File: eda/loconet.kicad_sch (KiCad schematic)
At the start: 68 parts, among them J1 RJ12, J10 FROG4, J11 LN Debug, J12 LN Raw, J13 12V IN, J2 DCC IN, J3 FROG1, J4 DCC1, J5 FROG2, J6 DCC2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

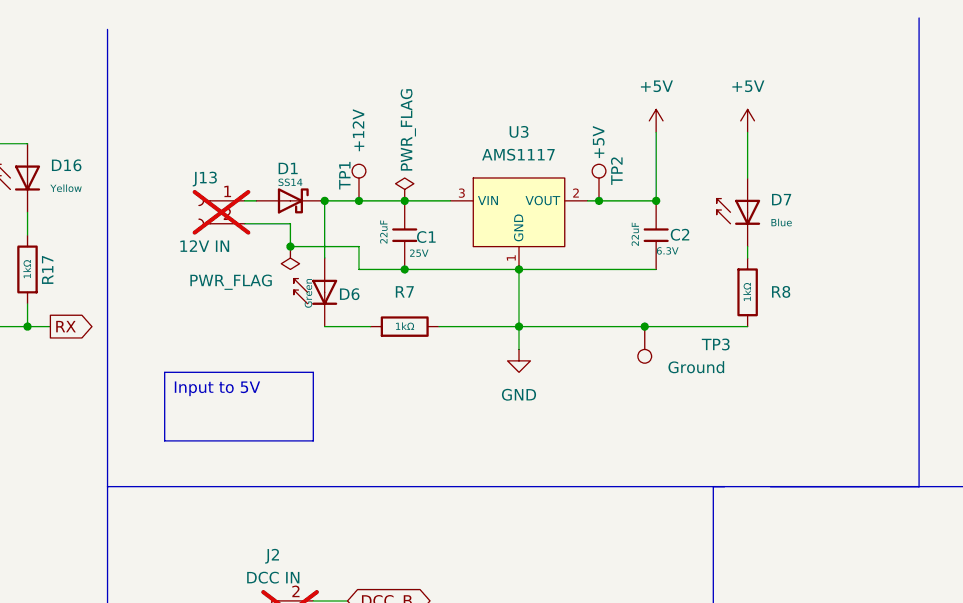
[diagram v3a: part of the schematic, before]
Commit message: Design fixups
* LDO was too limited in input voltage, switch to a part with a bigger input voltage
* Update README
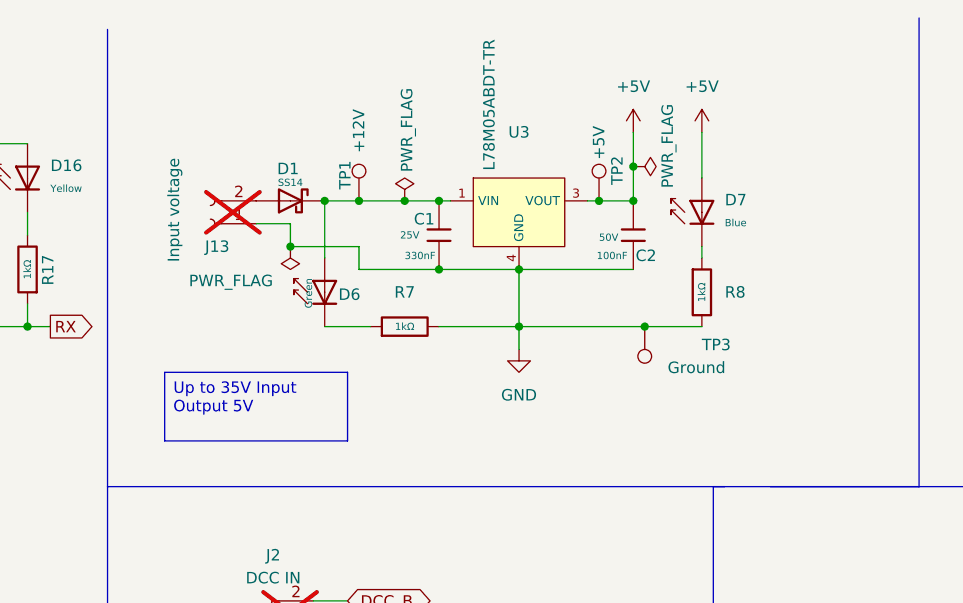
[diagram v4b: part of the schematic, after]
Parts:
- removed C1: 22uF, PCM_JLCPCB:C_0805, symbol PCM_JLCPCB-Capacitors:0805,22uF
- removed C2: 22uF, PCM_JLCPCB:C_0603, symbol PCM_JLCPCB-Capacitors:0603,22uF
- removed U3: AMS1117, PCM_JLCPCB:SOT-223_L6.5-W3.5-P2.30-LS7.0-BR, symbol PCM_JLCPCB-Power:LDO, 5V, 1A
- added C1: 330nF, PCM_JLCPCB:C_0603, symbol PCM_JLCPCB-Capacitors:0603,330nF
- added C2: 100nF, PCM_JLCPCB:C_0603, symbol PCM_JLCPCB-Capacitors:0603,100nF
- added U3: L78M05ABDT-TR, PCM_JLCPCB:TO-252-2_L6.5-W6.1-P4.58-LS10.0-TL, symbol PCM_JLCPCB-Power:LDO, 5V, 0.5A
- J13: value 12V IN -> Input voltage
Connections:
- net +5V: now also C2.1, U3.3 (VOUT)
- net GND: now also J13.1 (Pin_1), C1.2, C2.2, U3.4 (GND); no longer J13.2 (Pin_2)
- net at D1.2: now also J13.2 (Pin_2); no longer J13.1 (Pin_1)
- net at D1.1, D6.2, TP1.1: now also C1.1, U3.1 (VIN)
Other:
- moved on the sheet: D7, J13, R8

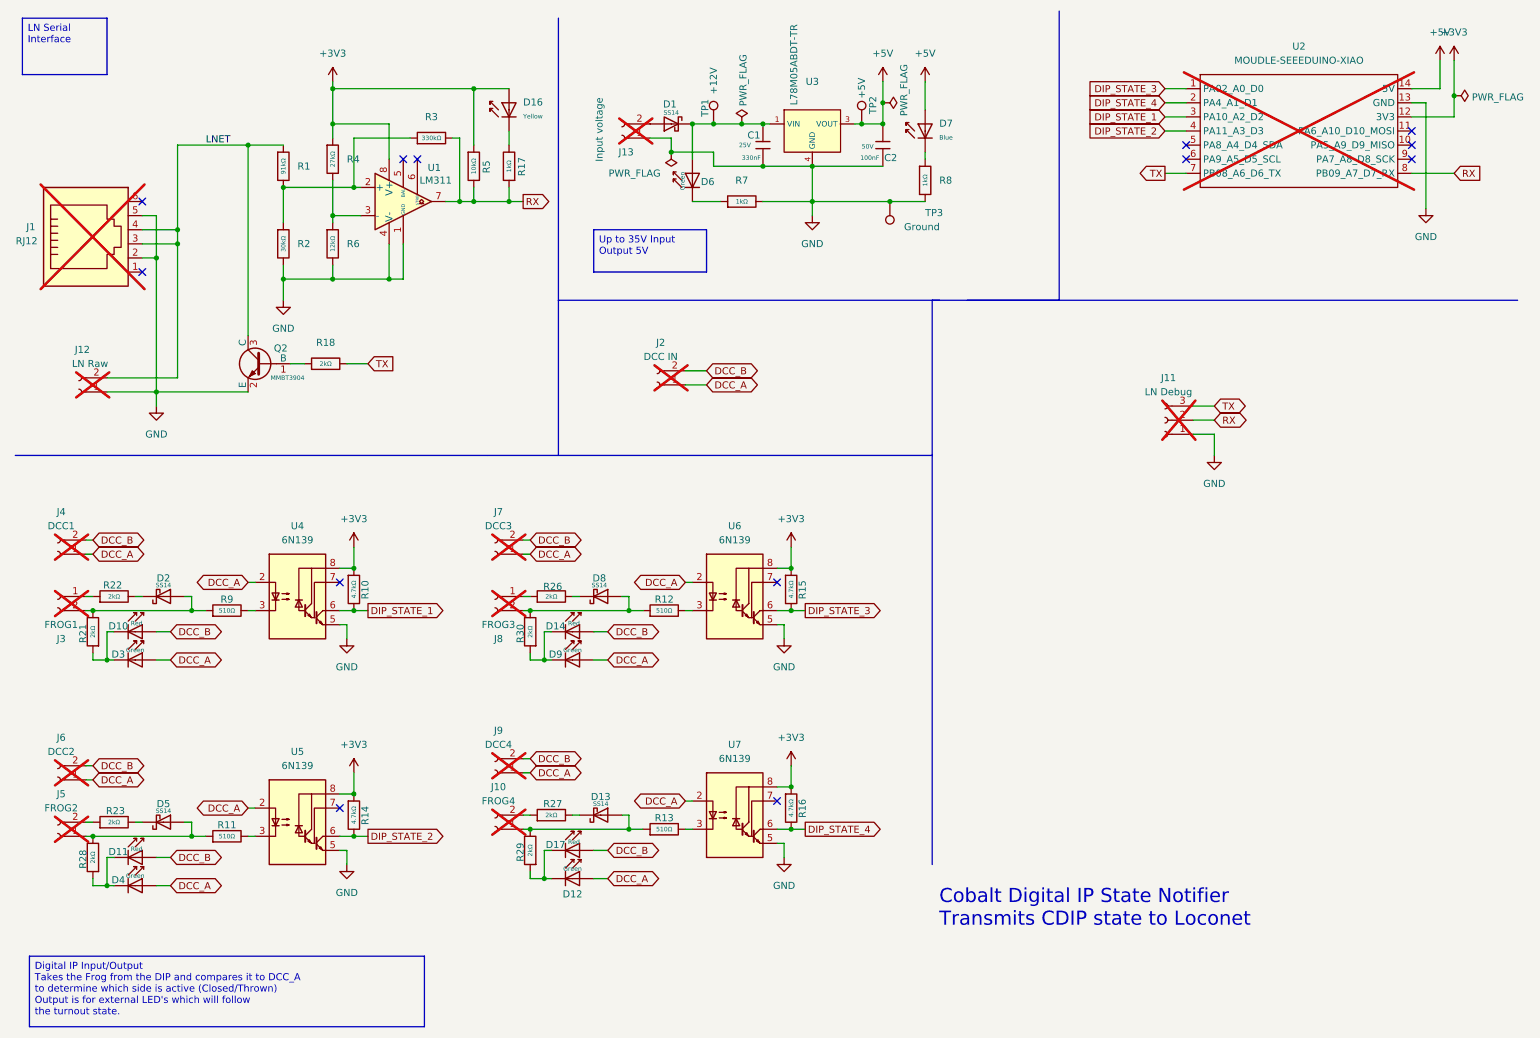
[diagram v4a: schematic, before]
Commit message: Updates
* Made it possible to power with DCC. You still need a DCC input for the IO, but you can also drive this with DCC.
* Added some screen printing for help
* Added 3 GPIO headers. You can connect them how you want, but they aren't protected, so don't do anything dumb.
* updated readme
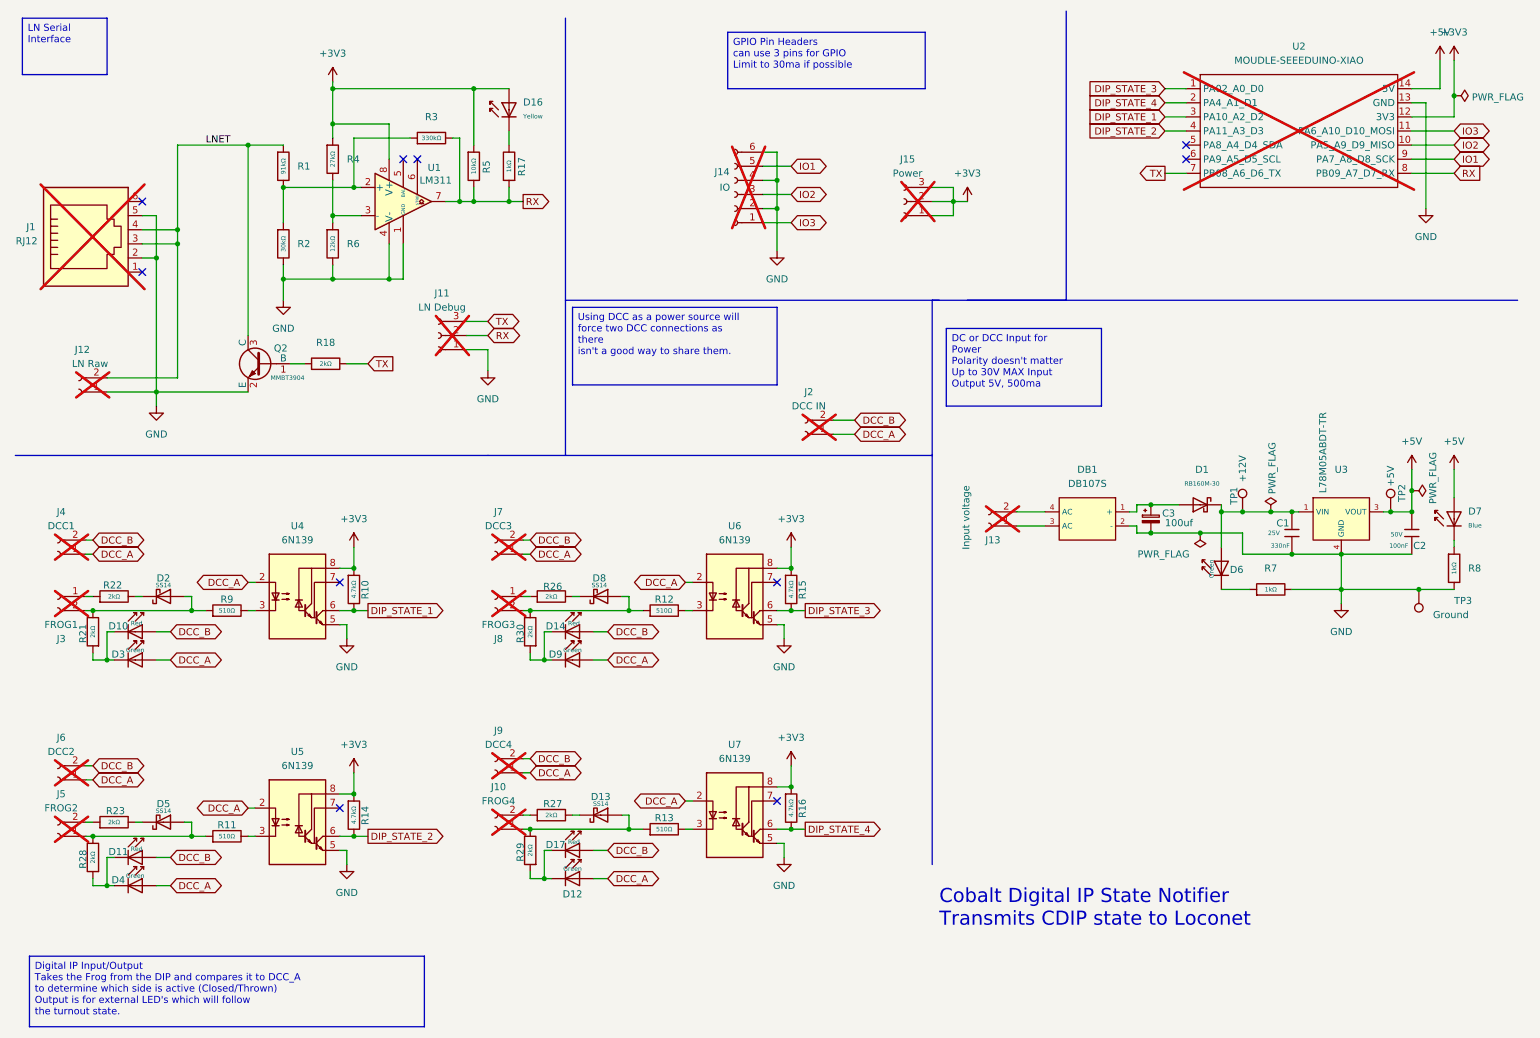
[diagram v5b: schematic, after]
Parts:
- removed D1: SS14, PCM_JLCPCB:D_SMA, symbol PCM_JLCPCB-Diodes:Schottky,SS14
- added C3: 100uf, Capacitor_THT:CP_Radial_D5.0mm_P2.50mm, symbol Device:C_Polarized_Small
- added D1: RB160M-30, PCM_JLCPCB:D_SOD-123, symbol PCM_JLCPCB-Diodes:Schottky,RB160M-30
- added DB1: DB107S, PCM_JLCPCB:DBS_L8.2-W6.4-P5.10-LS10.0-BL, symbol PCM_JLCPCB-Diode-Packages:Bridge Rectifier, DB107S
- added J14: IO, Connector_PinHeader_2.54mm:PinHeader_2x03_P2.54mm_Vertical, symbol Connector:Conn_01x06_Socket
- added J15: Power, Connector_PinHeader_2.54mm:PinHeader_1x03_P2.54mm_Vertical, symbol Connector:Conn_01x03_Socket
- J1: footprint Connector_RJ:RJ12_Amphenol_54601-x06_Horizontal -> Connector_RJ:RJ25_Wayconn_MJEA-660X1_Horizontal
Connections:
- net +3V3: now also J15.1 (Pin_1), J15.2 (Pin_2), J15.3 (Pin_3)
- net GND: now also C3.2, DB1.2 (-), J14.2 (Pin_2), J14.4 (Pin_4), J14.6 (Pin_6); no longer J13.1 (Pin_1)
- net at J13.2 (Pin_2): now also DB1.4 (AC)
- net at C1.1, D6.2, TP1.1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: now also D1.1
- net IO2: now reaches U2.10 (PA5_A9_D9_MISO)
- net IO2: now also J14.3 (Pin_3)
- net IO3: now reaches U2.11 (PA6_A10_D10_MOSI)
- net IO3: now also J14.1 (Pin_1)
- net IO1: now reaches U2.9 (PA7_A8_D8_SCK)
- net IO1: now also J14.5 (Pin_5)
- new net: C3.1, D1.2, DB1.1 (+)
- new net: DB1.3 (AC), J13.1 (Pin_1)
- no-connect marks 13 -> 10
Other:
- moved on the sheet: C1, C2, D6, D7, J11, J13, J2, R7, R8, TP1, TP2, TP3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

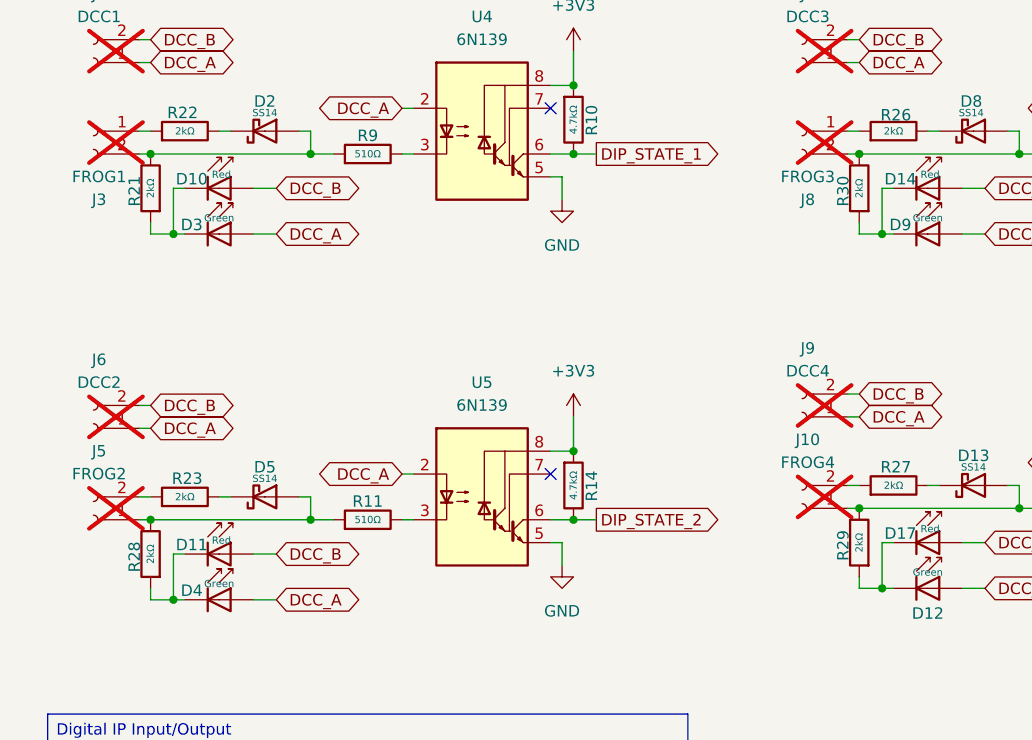
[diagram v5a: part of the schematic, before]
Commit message: Fixes
* Bumped the turnout indicator LED resistor to a 125mw 0805 as the 62.5mw was likely going to be too small. This allows some headroom.
* Updated README.
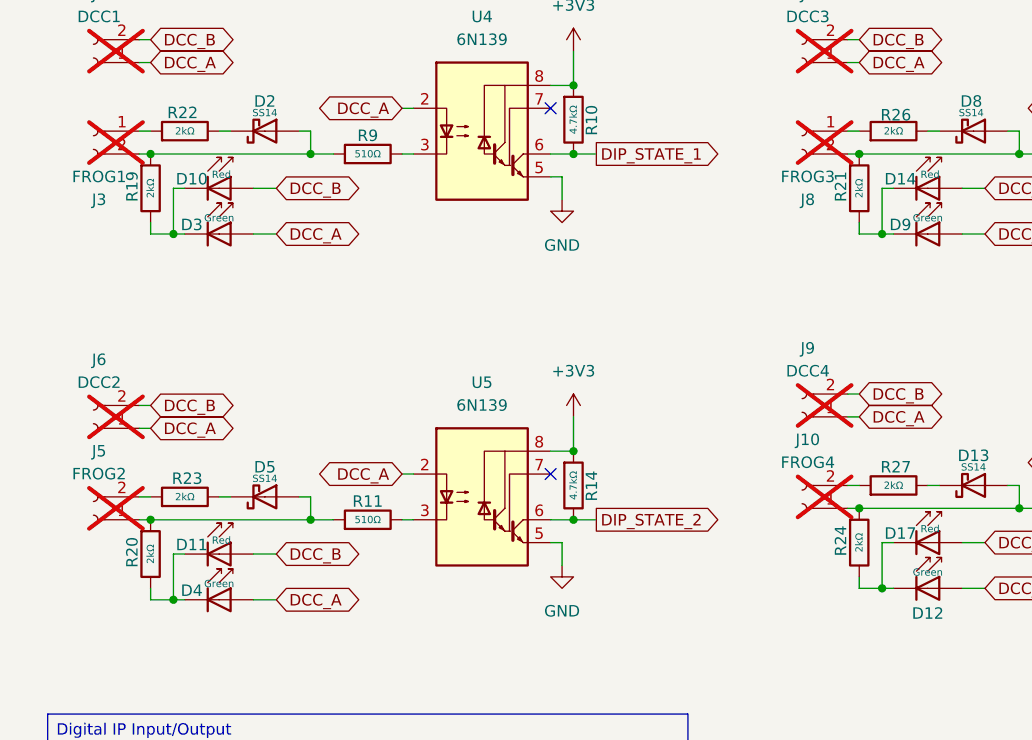
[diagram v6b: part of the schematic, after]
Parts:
- removed R21, R28, R29, R30: 2kΩ, PCM_JLCPCB:R_0402, symbol PCM_JLCPCB-Resistors:0402,2kΩ
- added R19, R20, R21, R24: 2kΩ, PCM_JLCPCB:R_0805, symbol PCM_JLCPCB-Resistors:0805,2kΩ
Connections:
- net at D14.1, D9.1: now also R21.2
- net at D8.2, J8.2 (Pin_2), R12.1: now also R21.1
- net at D10.1, D3.1: now also R19.2
- net at D2.2, J3.2 (Pin_2), R9.1: now also R19.1
- net at D5.2, J5.1 (Pin_1), R11.1: now also R20.1
- net at D13.2, J10.1 (Pin_1), R13.1: now also R24.1
- net at D11.1, D4.1: now also R20.2
- net at D12.1, D17.1: now also R24.2

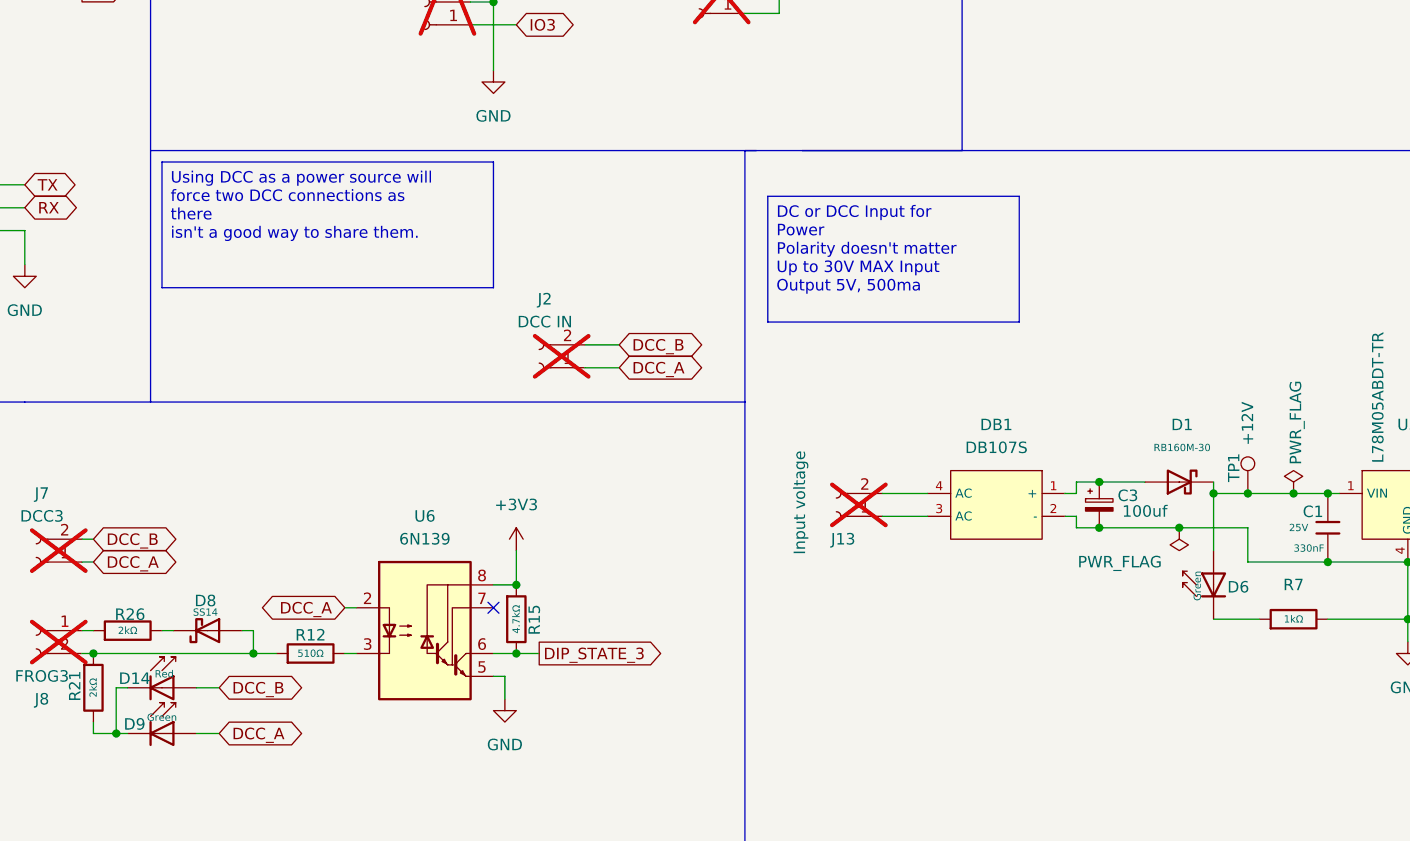
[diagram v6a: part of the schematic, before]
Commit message: checkpoint, as this board is too expensive.
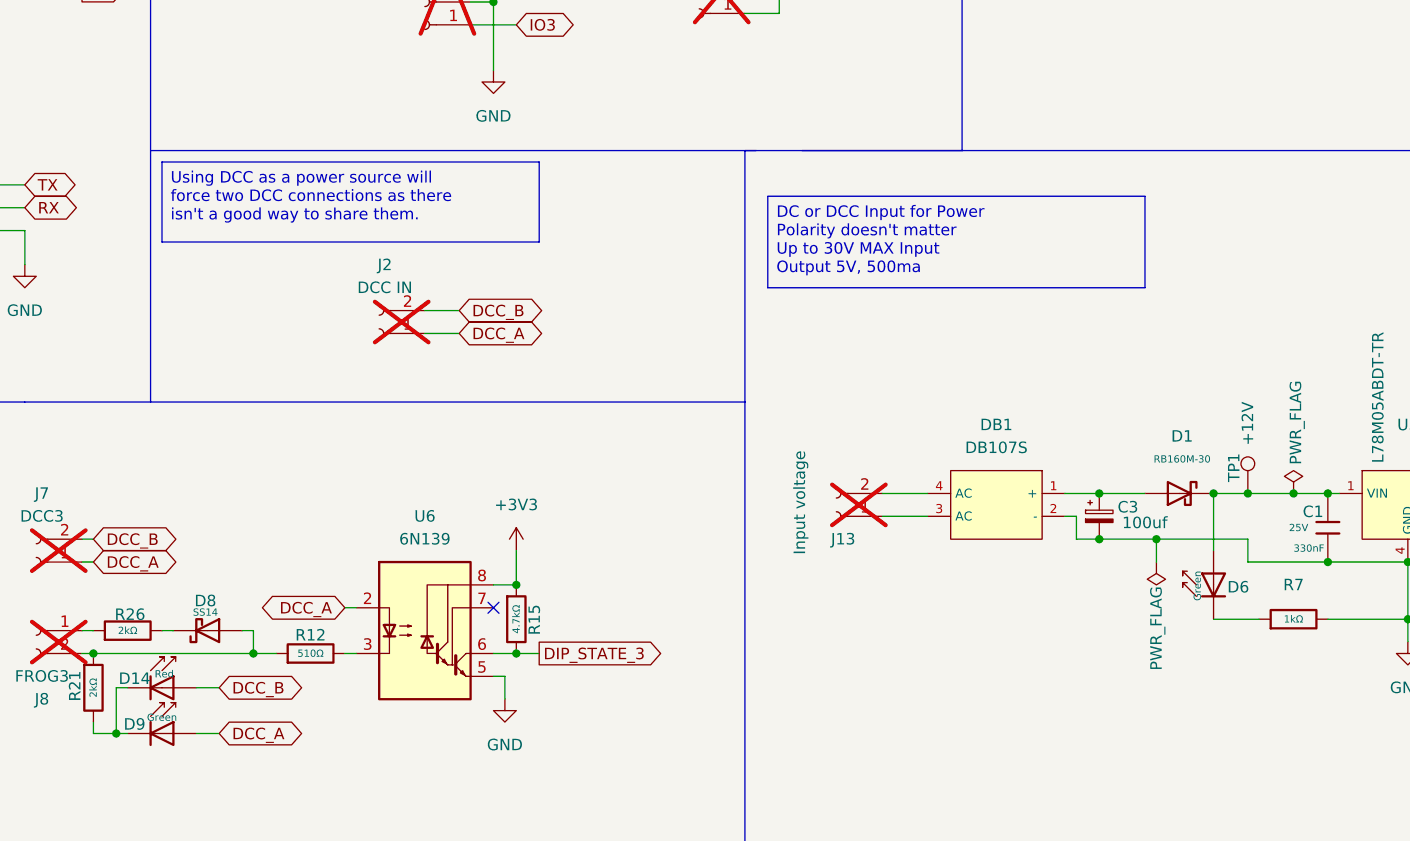
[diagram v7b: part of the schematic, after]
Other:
- moved on the sheet: C3, D1, J2

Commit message: Remove the barrel cap from the BOM.
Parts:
- TP1, TP2, TP3: now left out of the parts list
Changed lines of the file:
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@@
 		(unit 1)
 		(exclude_from_sim no)
-		(in_bom yes)
+		(in_bom no)
 		(on_board yes)
 		(dnp no)
@@
 		(unit 1)
 		(exclude_from_sim no)
-		(in_bom yes)
+		(in_bom no)
 		(on_board yes)
 		(dnp no)
@@
 		(unit 1)
 		(exclude_from_sim no)
-		(in_bom yes)
+		(in_bom no)
 		(on_board yes)
 		(dnp no)
